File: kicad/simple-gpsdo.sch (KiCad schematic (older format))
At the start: 92 parts, among them J1 PPS_OUT, J2 PWR, J3 ISP, J6 USB_B_Micro, J7 NEO-6M, J8 10MHz_OUT, Q1 PJA3407, SW1 RST, U1 XRP6272ITC5TR-F, U2 ATmega32U4-AU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

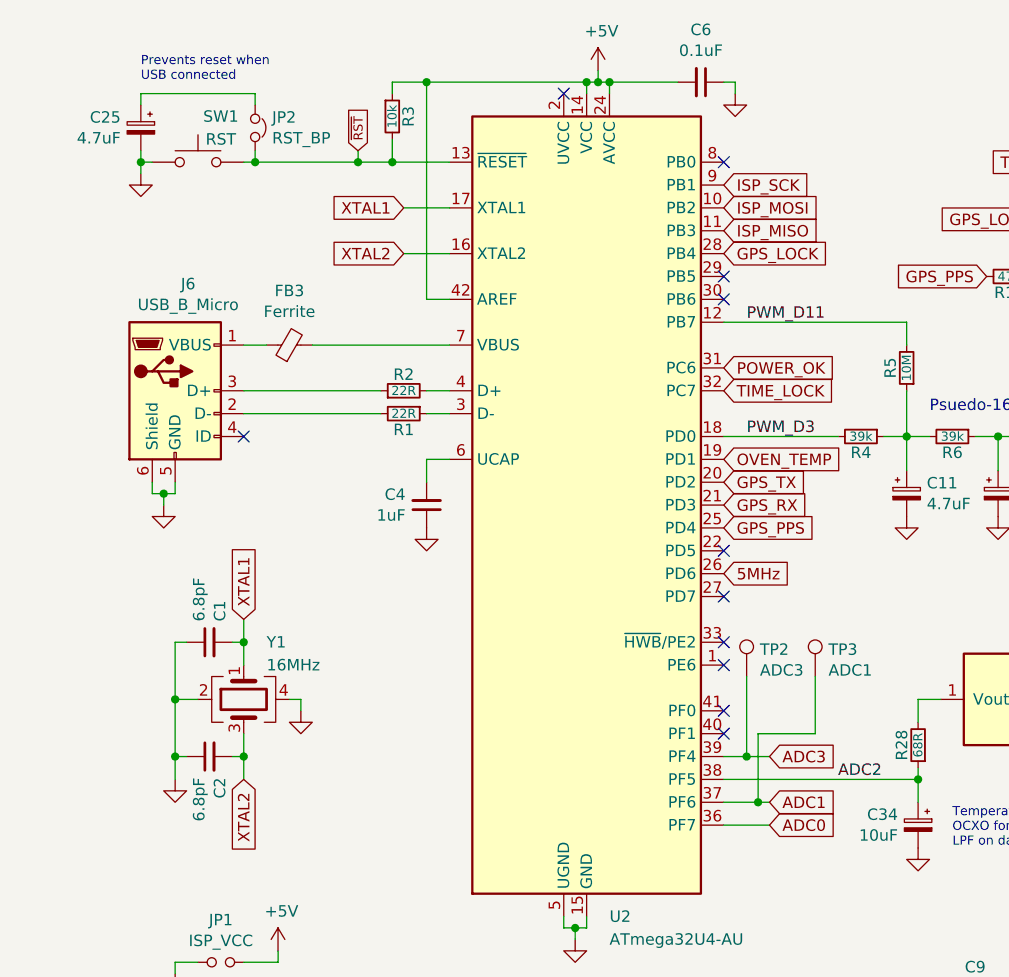
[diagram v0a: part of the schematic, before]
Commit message: revision E updates
added external 1.2 VREF
connected UVCC to VCC
switched pins for 5MHz, PPS, and LEDs to work properly
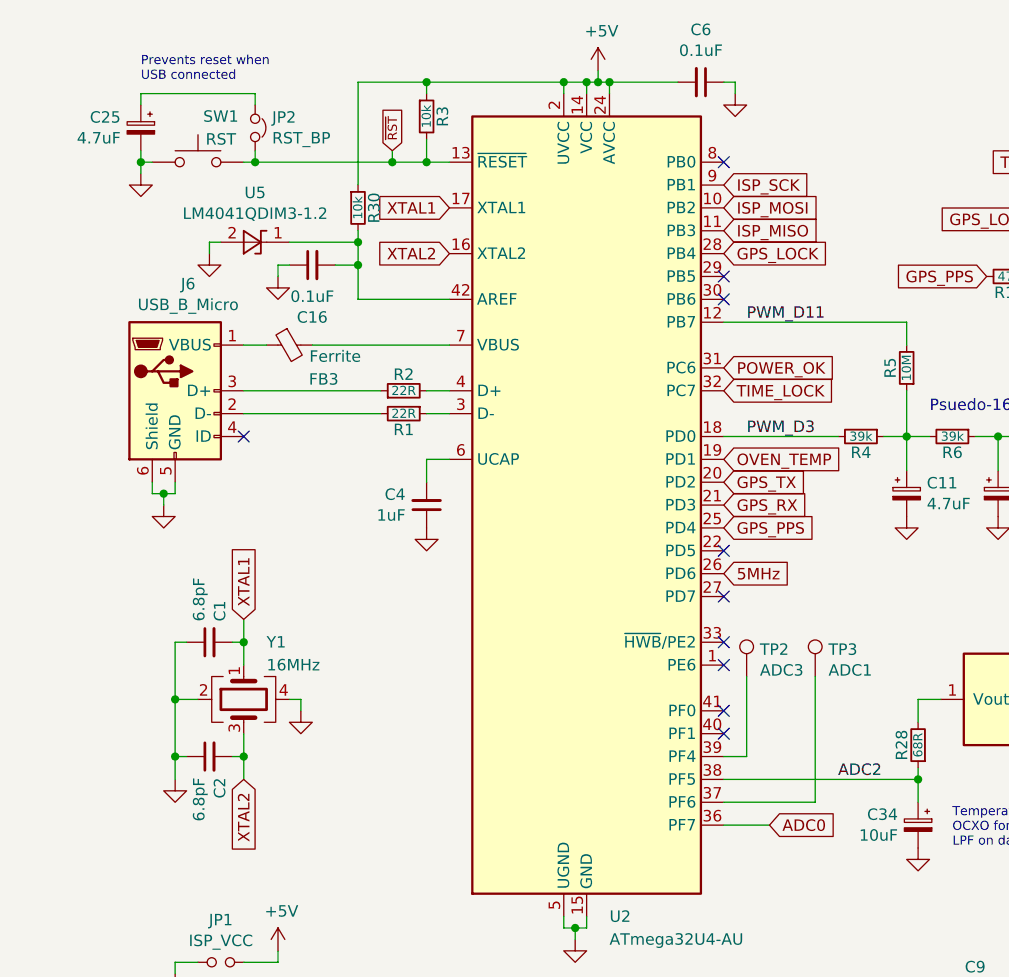
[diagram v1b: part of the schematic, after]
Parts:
- added C16: 0.1uF, Capacitor_SMD:C_0805_2012Metric_Pad1.15x1.40mm_HandSolder, symbol Device:C_Small
- added R30: 10k, Resistor_SMD:R_0805_2012Metric_Pad1.15x1.40mm_HandSolder, symbol Device:R_Small
- added U5: LM4041QDIM3-1.2, Package_TO_SOT_SMD:SOT-23, symbol Reference_Voltage:LM4040DBZ-2.5
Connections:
- net +5V: now also U2.2 (UVCC), R30.1; no longer U2.42 (AREF)
- net GND: now also C16.1, U5.2 (A)
- net ADC1: no longer names the net of TP3.1, U2.37 (PF6)
- net ADC3: no longer names the net of TP2.1, U2.39 (PF4)
- new net: C16.2, R30.2, U2.42 (AREF), U5.1 (K)
- no-connect marks 14 -> 13
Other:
- moved on the sheet: R3
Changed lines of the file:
@@
 Sheet 1 1
 Title "Simple GPSDO"
-Date "2021-10-23"
-Rev "D"
+Date "2021-11-04"
+Rev "E"
 Comp "W3AXL"
 Comment1 ""
@@
 	0    1    1    0
 $EndComp
-NoConn ~ 3400 1200
-Wire Wire Line
-	2800 2100 2800 1150
-Wire Wire Line
-	2800 1150 3500 1150
 Connection ~ 3500 1150
 $Comp
@@
 L Device:R_Small R3
 U 1 1 5F6CE40C
-P 2650 1300
-F 0 "R3" V 2750 1300 50  0000 C BNN
-F 1 "10k" V 2650 1300 40  0000 C CNN
-F 2 "Resistor_SMD:R_0805_2012Metric_Pad1.15x1.40mm_HandSolder" H 2650 1300 50  0001 C CNN
-F 3 "~" H 2650 1300 50  0001 C CNN
-	1    2650 1300
-	1    0    0    -1
-$EndComp
-Wire Wire Line
-	2650 1400 2650 1500
-Connection ~ 2650 1500
-Wire Wire Line
-	2650 1200 2650 1150
-Wire Wire Line
-	2650 1150 2800 1150
-Connection ~ 2800 1150
+P 2800 1300
+F 0 "R3" V 2900 1300 50  0000 C BNN
+F 1 "10k" V 2800 1300 40  0000 C CNN
+F 2 "Resistor_SMD:R_0805_2012Metric_Pad1.15x1.40mm_HandSolder" H 2800 1300 50  0001 C CNN
+F 3 "~" H 2800 1300 50  0001 C CNN
+	1    2800 1300
+	1    0    0    -1
+$EndComp
+Wire Wire Line
+	2800 1400 2800 1500
 $Comp
 L Device:C_Small C4
@@
 	1    0    0    -1
 $EndComp
-Text GLabel 2500 1450 1    40   Input ~ 0
+Text GLabel 2650 1450 1    40   Input ~ 0
 ~RST
 Text GLabel 4100 1800 2    50   Input ~ 0
@@
 PWM_D11
 NoConn ~ 4100 2000
-Text GLabel 4300 4100 2    50   Input ~ 0
-ADC3
-Text GLabel 4300 4300 2    50   Input ~ 0
-ADC1
-Wire Wire Line
-	4100 4300 4250 4300
 Wire Wire Line
 	4100 4400 4300 4400
-Wire Wire Line
-	4300 4100 4200 4100
 $Comp
 L Connector:TestPoint TP3
@@
 	1    0    0    -1
 $EndComp
-Connection ~ 4200 4100
 Wire Wire Line
 	4200 4100 4100 4100
 Wire Wire Line
 	4200 3750 4200 4100
-Wire Wire Line
-	4250 4300 4250 4000
-Wire Wire Line
-	4250 4000 4500 4000
-Wire Wire Line
-	4500 4000 4500 3750
-Connection ~ 4250 4300
-Wire Wire Line
-	4250 4300 4300 4300
 Wire Wire Line
 	8400 1350 8500 1350
@@
 	1    0    0    -1
 $EndComp
-Text GLabel 2700 1700 0    50   Input ~ 0
+Text GLabel 2900 1700 0    50   Input ~ 0
 XTAL1
-Text GLabel 2700 1900 0    50   Input ~ 0
+Text GLabel 2900 1900 0    50   Input ~ 0
 XTAL2
 Wire Wire Line
@@
 	2900 2800 2800 2800
 Wire Wire Line
-	2900 2100 2800 2100
-Wire Wire Line
 	2800 2500 2900 2500
 Wire Wire Line
 	2900 2600 2800 2600
-Wire Wire Line
-	2900 1700 2700 1700
-Wire Wire Line
-	2700 1900 2900 1900
-Wire Wire Line
-	2650 1500 2900 1500
 Connection ~ 2000 4100
 Wire Wire Line
@@
 Connection ~ 1550 1500
 Wire Wire Line
-	2050 1500 2500 1500
-Wire Wire Line
-	2500 1450 2500 1500
-Connection ~ 2500 1500
-Wire Wire Line
-	2500 1500 2650 1500
+	2650 1450 2650 1500
 Wire Wire Line
 	2000 2500 2600 2500
@@
 U 1 1 623A3FC5
 P 2200 2300
-F 0 "FB3" V 2437 2300 50  0000 C CNN
-F 1 "Ferrite" V 2346 2300 50  0000 C CNN
+F 0 "FB3" V 2350 2150 50  0000 C CNN
+F 1 "Ferrite" V 2250 2100 50  0000 C CNN
 F 2 "Fuse:Fuse_1206_3216Metric_Pad1.42x1.75mm_HandSolder" V 2130 2300 50  0001 C CNN
 F 3 "~" H 2200 2300 50  0001 C CNN
 	1    2200 2300
-	0    -1   -1   0
+	0    -1   1    0
 $EndComp
 Wire Wire Line
@@
 $EndComp
 Connection ~ 5700 6650
+NoConn ~ 4100 3200
 $Comp
 L simple-gpsdo-rescue:ATmega32U4-AU-MCU_Microchip_ATmega U2
@@
 	1    0    0    -1
 $EndComp
-NoConn ~ 4100 3200
+Wire Wire Line
+	3400 1200 3400 1150
+Connection ~ 3400 1150
+Wire Wire Line
+	3400 1150 3500 1150
+Wire Wire Line
+	2500 2100 2900 2100
+$Comp
+L Reference_Voltage:LM4040DBZ-2.5 U5
+U 1 1 61920BAC
+P 2050 1850
+F 0 "U5" H 2050 2066 50  0000 C CNN
+F 1 "LM4041QDIM3-1.2" H 2050 1975 50  0000 C CNN
+F 2 "Package_TO_SOT_SMD:SOT-23" H 2050 1650 50  0001 C CIN
+F 3 "http://www.ti.com/lit/ds/symlink/lm4040-n.pdf" H 2050 1850 50  0001 C CIN
+	1    2050 1850
+	1    0    0    -1
+$EndComp
+Connection ~ 2800 1500
+Wire Wire Line
+	2800 1500 2900 1500
+Wire Wire Line
+	2800 1200 2800 1150
+Connection ~ 2800 1150
+Wire Wire Line
+	2800 1150 3400 1150
+Connection ~ 2650 1500
+Wire Wire Line
+	2650 1500 2800 1500
+Wire Wire Line
+	2050 1500 2650 1500
+$Comp
+L Device:R_Small R30
+U 1 1 6196FBBC
+P 2500 1700
+F 0 "R30" V 2600 1700 50  0000 C BNN
+F 1 "10k" V 2500 1700 40  0000 C CNN
+F 2 "Resistor_SMD:R_0805_2012Metric_Pad1.15x1.40mm_HandSolder" H 2500 1700 50  0001 C CNN
+F 3 "~" H 2500 1700 50  0001 C CNN
+	1    2500 1700
+	1    0    0    -1
+$EndComp
+Wire Wire Line
+	2500 1800 2500 1850
+Wire Wire Line
+	1900 1850 1850 1850
+Wire Wire Line
+	2500 1150 2500 1600
+Wire Wire Line
+	2500 1150 2800 1150
+Connection ~ 2500 1850
+Wire Wire Line
+	2200 1850 2500 1850
+Wire Wire Line
+	4500 3750 4500 4300
+Wire Wire Line
+	4100 4300 4500 4300
+$Comp
+L Device:C_Small C16
+U 1 1 61A61801
+P 2300 1950
+F 0 "C16" V 2071 1950 50  0000 C CNN
+F 1 "0.1uF" V 2162 1950 50  0000 C CNN
+F 2 "Capacitor_SMD:C_0805_2012Metric_Pad1.15x1.40mm_HandSolder" H 2300 1950 50  0001 C CNN
+F 3 "~" H 2300 1950 50  0001 C CNN
+	1    2300 1950
+	0    -1   -1   0
+$EndComp
+Wire Wire Line
+	2500 1850 2500 1950
+Wire Wire Line
+	1850 1850 1850 1900
+$Comp
+L power:GND #PWR036
+U 1 1 619B77AC
+P 1850 1900
+F 0 "#PWR036" H 1850 1650 50  0001 C CNN
+F 1 "GND" H 1855 1727 50  0001 C CNN
+F 2 "" H 1850 1900 50  0001 C CNN
+F 3 "" H 1850 1900 50  0001 C CNN
+	1    1850 1900
+	1    0    0    -1
+$EndComp
+$Comp
+L power:GND #PWR039
+U 1 1 61AB7055
+P 2150 2000
+F 0 "#PWR039" H 2150 1750 50  0001 C CNN
+F 1 "GND" H 2155 1827 50  0001 C CNN
+F 2 "" H 2150 2000 50  0001 C CNN
+F 3 "" H 2150 2000 50  0001 C CNN
+	1    2150 2000
+	1    0    0    -1
+$EndComp
+Wire Wire Line
+	2200 1950 2150 1950
+Wire Wire Line
+	2150 1950 2150 2000
+Wire Wire Line
+	2400 1950 2500 1950
+Connection ~ 2500 1950
+Wire Wire Line
+	2500 1950 2500 2100
 $EndSCHEMATC

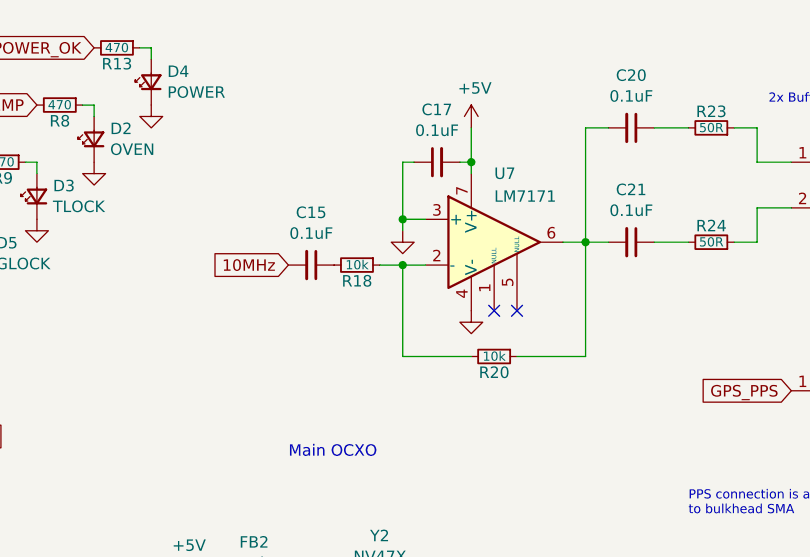
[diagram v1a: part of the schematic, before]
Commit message: Updates to output amplifier, added simulation
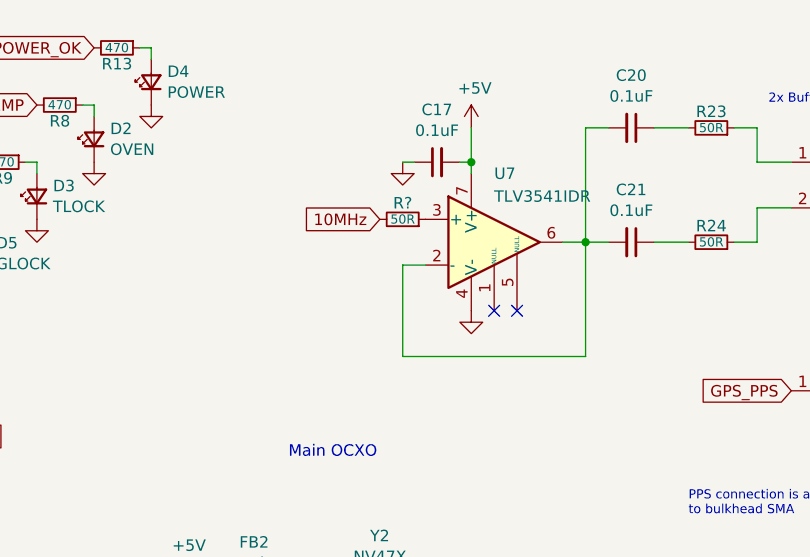
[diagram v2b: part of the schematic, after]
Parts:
- removed C15: 0.1uF, Capacitor_SMD:C_0805_2012Metric_Pad1.15x1.40mm_HandSolder, symbol Device:C_Small
- removed R18, R20: 10k, Resistor_SMD:R_0805_2012Metric_Pad1.15x1.40mm_HandSolder, symbol Device:R_Small
- added R?: 50R, Resistor_SMD:R_0805_2012Metric_Pad1.15x1.40mm_HandSolder, symbol Device:R_Small
- U7: value LM7171 -> TLV3541IDR
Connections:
- net 10MHz: now also R?.2
- net GND: no longer U7.3 (+)
- net at U7.2 (-): now also C20.2, C21.2, U7.6
- new net: R?.1, U7.3 (+)
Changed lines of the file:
@@
 Text GLabel 4100 1900 2    50   Input ~ 0
 GPS_LOCK
-Text GLabel 7100 1950 0    50   Input ~ 0
-10MHz
 NoConn ~ 4100 2100
 NoConn ~ 4100 3600
@@
 P 8000 1850
 F 0 "U7" H 8000 2150 50  0000 L CNN
-F 1 "LM7171" H 8000 2050 50  0000 L CNN
+F 1 "TLV3541IDR" H 8000 2050 50  0000 L CNN
 F 2 "Package_SO:SOIC-8_3.9x4.9mm_P1.27mm" H 8050 1900 50  0001 C CNN
 F 3 "https://www.analog.com/media/en/technical-documentation/data-sheets/AD8610_8620.pdf" H 8150 2000 50  0001 C CNN
@@
 $EndComp
 $Comp
-L Device:R_Small R18
-U 1 1 5F835714
-P 7400 1950
-F 0 "R18" V 7500 1950 50  0000 C BNN
-F 1 "10k" V 7400 1950 40  0000 C CNN
-F 2 "Resistor_SMD:R_0805_2012Metric_Pad1.15x1.40mm_HandSolder" H 7400 1950 50  0001 C CNN
-F 3 "~" H 7400 1950 50  0001 C CNN
-	1    7400 1950
-	0    1    1    0
-$EndComp
-$Comp
 L power:GND #PWR043
 U 1 1 5F857189
-P 7600 1800
-F 0 "#PWR043" H 7600 1550 50  0001 C CNN
-F 1 "GND" H 7605 1627 50  0001 C CNN
-F 2 "" H 7600 1800 50  0001 C CNN
-F 3 "" H 7600 1800 50  0001 C CNN
-	1    7600 1800
+P 7600 1500
+F 0 "#PWR043" H 7600 1250 50  0001 C CNN
+F 1 "GND" H 7605 1327 50  0001 C CNN
+F 2 "" H 7600 1500 50  0001 C CNN
+F 3 "" H 7600 1500 50  0001 C CNN
+	1    7600 1500
 	1    0    0    -1
 $EndComp
@@
 	7900 1500 7900 1550
 Wire Wire Line
-	7500 1950 7600 1950
-Wire Wire Line
 	7650 1500 7600 1500
 Wire Wire Line
-	7600 1500 7600 1750
-Wire Wire Line
-	7700 1750 7600 1750
-Connection ~ 7600 1750
-Wire Wire Line
-	7600 1750 7600 1800
-Wire Wire Line
 	7900 1350 7900 1500
-$Comp
-L Device:R_Small R20
-U 1 1 5F89FD3A
-P 8000 2350
-F 0 "R20" V 8100 2350 50  0000 C BNN
-F 1 "10k" V 8000 2350 40  0000 C CNN
-F 2 "Resistor_SMD:R_0805_2012Metric_Pad1.15x1.40mm_HandSolder" H 8000 2350 50  0001 C CNN
-F 3 "~" H 8000 2350 50  0001 C CNN
-	1    8000 2350
-	0    1    1    0
-$EndComp
 NoConn ~ 8000 2150
 NoConn ~ 8100 2150
@@
 	1    0    0    -1
 $EndComp
-Wire Wire Line
-	7600 1950 7600 2350
-Wire Wire Line
-	7600 2350 7900 2350
-Connection ~ 7600 1950
-Wire Wire Line
-	7600 1950 7700 1950
-Wire Wire Line
-	8100 2350 8400 2350
-Wire Wire Line
-	8400 2350 8400 1850
 Wire Wire Line
 	8400 1850 8300 1850
@@
 Wire Wire Line
 	9150 1850 9050 1850
-$Comp
-L Device:C_Small C15
-U 1 1 5F9CF383
-P 7200 1950
-F 0 "C15" V 6971 1950 50  0000 C CNN
-F 1 "0.1uF" V 7062 1950 50  0000 C CNN
-F 2 "Capacitor_SMD:C_0805_2012Metric_Pad1.15x1.40mm_HandSolder" H 7200 1950 50  0001 C CNN
-F 3 "~" H 7200 1950 50  0001 C CNN
-	1    7200 1950
-	0    1    1    0
-$EndComp
 Text Notes 9200 1250 0    40   ~ 0
 2x Buffered 10MHz Outputs
@@
 Wire Wire Line
 	2500 1950 2500 2100
+Text GLabel 7500 1750 0    50   Input ~ 0
+10MHz
+Wire Wire Line
+	7600 1950 7700 1950
+Wire Wire Line
+	7600 1950 7600 2350
+Wire Wire Line
+	7600 2350 8400 2350
+Wire Wire Line
+	8400 2350 8400 1850
+$Comp
+L Device:R_Small R?
+U 1 1 618E603F
+P 7600 1750
+F 0 "R?" V 7700 1750 50  0000 C BNN
+F 1 "50R" V 7600 1750 40  0000 C CNN
+F 2 "Resistor_SMD:R_0805_2012Metric_Pad1.15x1.40mm_HandSolder" H 7600 1750 50  0001 C CNN
+F 3 "~" H 7600 1750 50  0001 C CNN
+	1    7600 1750
+	0    1    -1   0
+$EndComp
 $EndSCHEMATC
